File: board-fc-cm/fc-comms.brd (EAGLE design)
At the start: 100 x 100 mm, 231 parts, among them IC1 TXB0108PW, IC10 LNA_COMMON, IC2 LHA1+, IC3 MMZ09332BT1, IC4 PCT2075TP, IC5 PCT2075TP, IC6 MSP430FR2311PW, IC7 CC1125RHBT, IC8 CC1125RHBT, IC9 TXB0108PW, J1 SWD_SHROUD, Q1 8MHz, Q2 BSS84, Q3 32.768kHz, Q4 BSS123, Q5 BSS84, U1 TM4C123[7,G]XXPM, U2 TMP100-EP_DBV_6, U3 TPS3813K33-EP_DBV_6, U4 MPU-9250, U6 TPS79930QDDCRQ1, U7 TPS79930QDDCRQ1, U8 74LVC1G08, X1 BU-SMA-V, X10 BU-SMA-V, X11 BU-SMA-V, X12 BU-SMA-V, X14 BU-SMA-V, X15 BU-SMA-V, X16 BU-SMA-V, X17 BU-SMA-V, X18 SHIELD-26X26, X19 SHIELD-26X26, X2 BU-SMA-V, X20 LFTCXO070, X21 LFTCXO070, X3 BU-SMA-V, X4 BU-SMA-V, X5 BU-SMA-V, X6 BU-SMA-V, X7 BU-SMA-V, X8 BU-SMA-V, X9 BU-SMA-V

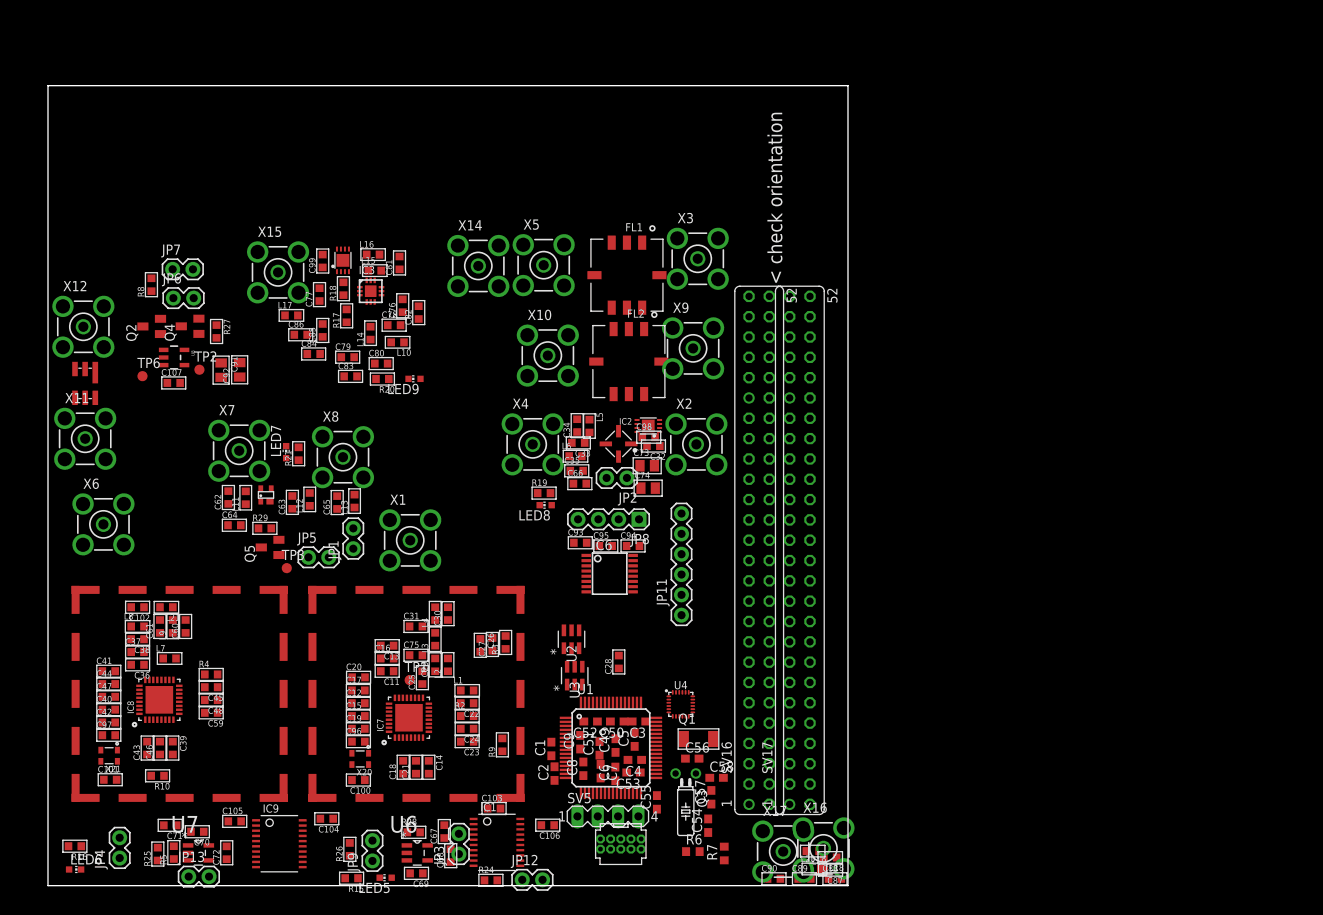
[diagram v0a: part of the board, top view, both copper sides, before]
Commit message: added outline and corrected header locations
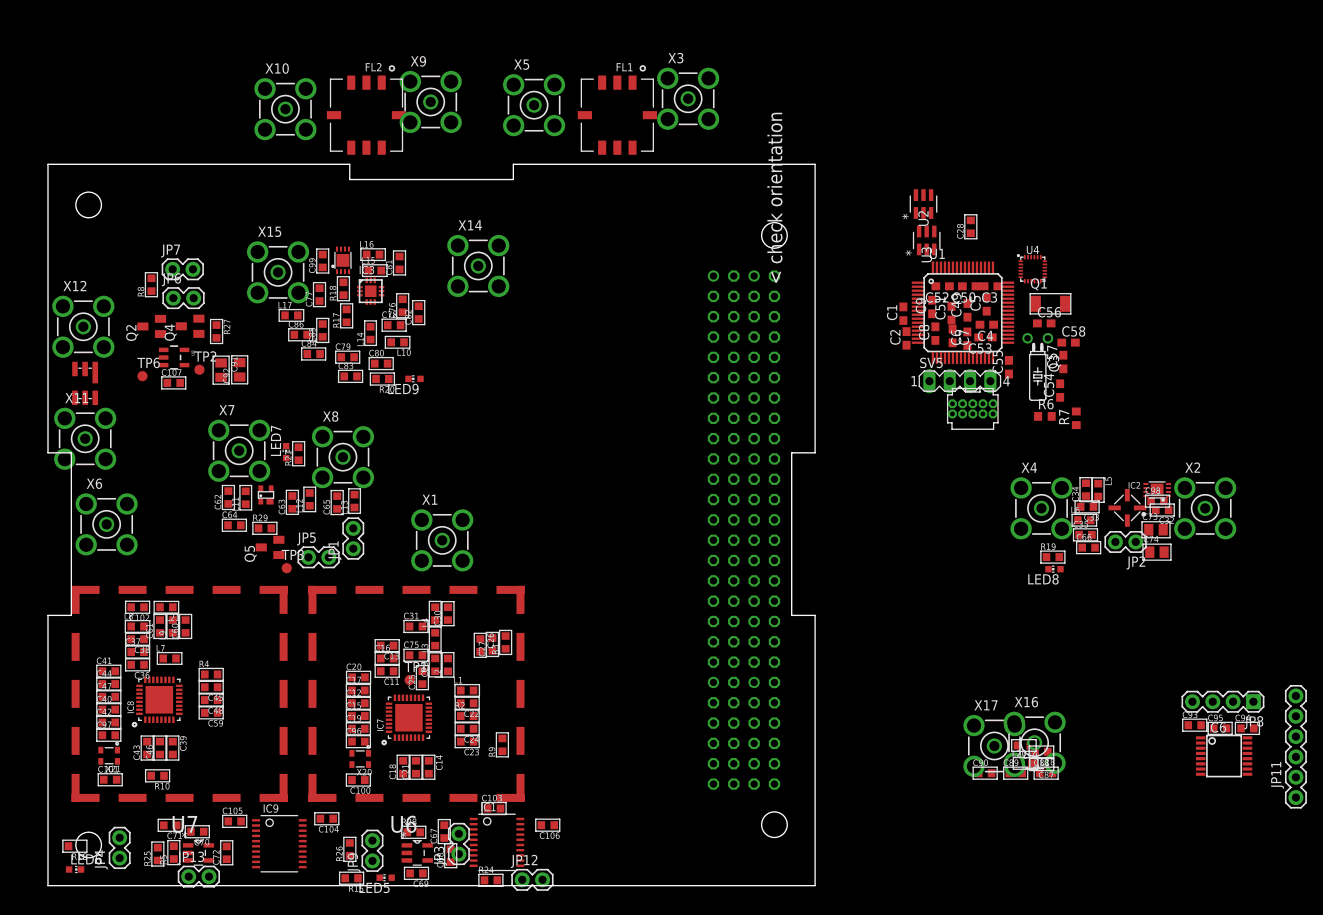
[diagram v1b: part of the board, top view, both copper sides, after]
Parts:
- added U$1: (no value), CubeSat3:OUTLINE
- moved C94 80.1 mm to (149.9, 19.7)
- moved C95 80.1 mm to (146.5, 19.7)
- moved JP11 80.1 mm to (156.0, 11.0)
- moved JP8 80.1 mm to (150.7, 23.0)
- moved C93 80.1 mm to (143.3, 20.1)
- moved IC6 80.1 mm to (147.0, 16.2)
- moved C3 70.0 mm to (117.9, 74.9)
- moved C4 70.0 mm to (117.3, 70.1)
- moved C50 70.0 mm to (115.2, 74.9)
- moved C51 70.0 mm to (112.9, 71.6)
- moved C52 70.0 mm to (111.8, 74.9)
- moved C53 70.0 mm to (117.2, 68.5)
- moved C55 70.0 mm to (120.1, 64.8)
- moved C57 70.0 mm to (126.9, 65.5)
- moved C6 70.0 mm to (114.9, 68.4)
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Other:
- board size 100 x 100 mm -> 95.9 x 90.2 mm

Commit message: more placement
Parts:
- added IC12: TXB0108PW, cube-parts:TSSOP20
- C1, C2, C3, C4, C49, C5, C50, C51, C52, C53, C54, C55, C56, C57, C58, C6, C7, C8, C9: device resistor:C0603 -> passives-7351:C0603-N
- R6, R7: device resistor:R0603 -> passives-7351:R0603-N
- moved C28 81.4 mm to (54.4, 28.4)
- moved C93 77.1 mm to (67.9, 3.74), turned to 90 degrees
- moved IC6 74.9 mm to (73.0, 4.60)
- moved C94 72.4 mm to (78.7, 6.73), turned to 90 degrees
- moved C54 69.7 mm to (63.7, 31.7), turned to 180 degrees
- moved C95 69.5 mm to (78.7, 4.12), turned to 90 degrees
- moved U4 67.7 mm to (60.0, 52.4), turned to 270 degrees
- moved C58 65.3 mm to (64.8, 50.0)
- moved C3 65.2 mm to (56.8, 52.0), turned to 270 degrees
- moved Q1 63.4 mm to (67.1, 47.7), turned to 180 degrees
- moved C6 61.7 mm to (60.8, 38.8), turned to 180 degrees
- moved C4 61.6 mm to (59.6, 48.8), turned to 0 degrees
- moved JP8 61.5 mm to (92.7, 2.59)
- moved C7 61.0 mm to (60.8, 37.2), turned to 180 degrees
- moved C57 60.9 mm to (68.0, 50.0), turned to 180 degrees
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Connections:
- removed net GND1: J1.3
- removed net GND2: J1.5
- removed net GNDD: J1.9
- removed net VCC: J1.1
- net !RST: now also J1.10
- net 3V3/FMCU: now also J1.1
- net GND: now also IC12.11, J1.3, J1.5, J1.9
- net SWCLK: now also J1.4
- net SWDIO: now also J1.2
- net SWO: now also J1.6
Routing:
- net SWO: track 0.00 -> 75.3 mm
- net SWCLK: track 0.00 -> 69.9 mm, vias 0 -> 1
- net !RST: track 0.00 -> 64.7 mm, vias 0 -> 1
- net GPIO4: track 0.00 -> 63.9 mm
- net GPIO3: track 0.00 -> 59.9 mm, vias 0 -> 1
- net GPIO1: track 0.00 -> 59.3 mm, vias 0 -> 1
- net GPIO5: track 0.00 -> 57.5 mm, vias 0 -> 1
- net GPIO2: track 0.00 -> 50.8 mm
- net N$63: track 0.00 -> 36.3 mm, vias 0 -> 1
- net PWR/INT: track 0.00 -> 30.0 mm, vias 0 -> 1
- net SWDIO: track 0.00 -> 30.0 mm
- net PWR/TXD: track 0.00 -> 26.8 mm, vias 0 -> 1
- net PWR/RXD: track 0.00 -> 25.9 mm, vias 0 -> 1
- net GND: track 0.00 -> 16.6 mm, vias 0 -> 4
- net N$101: track 0.00 -> 15.0 mm
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
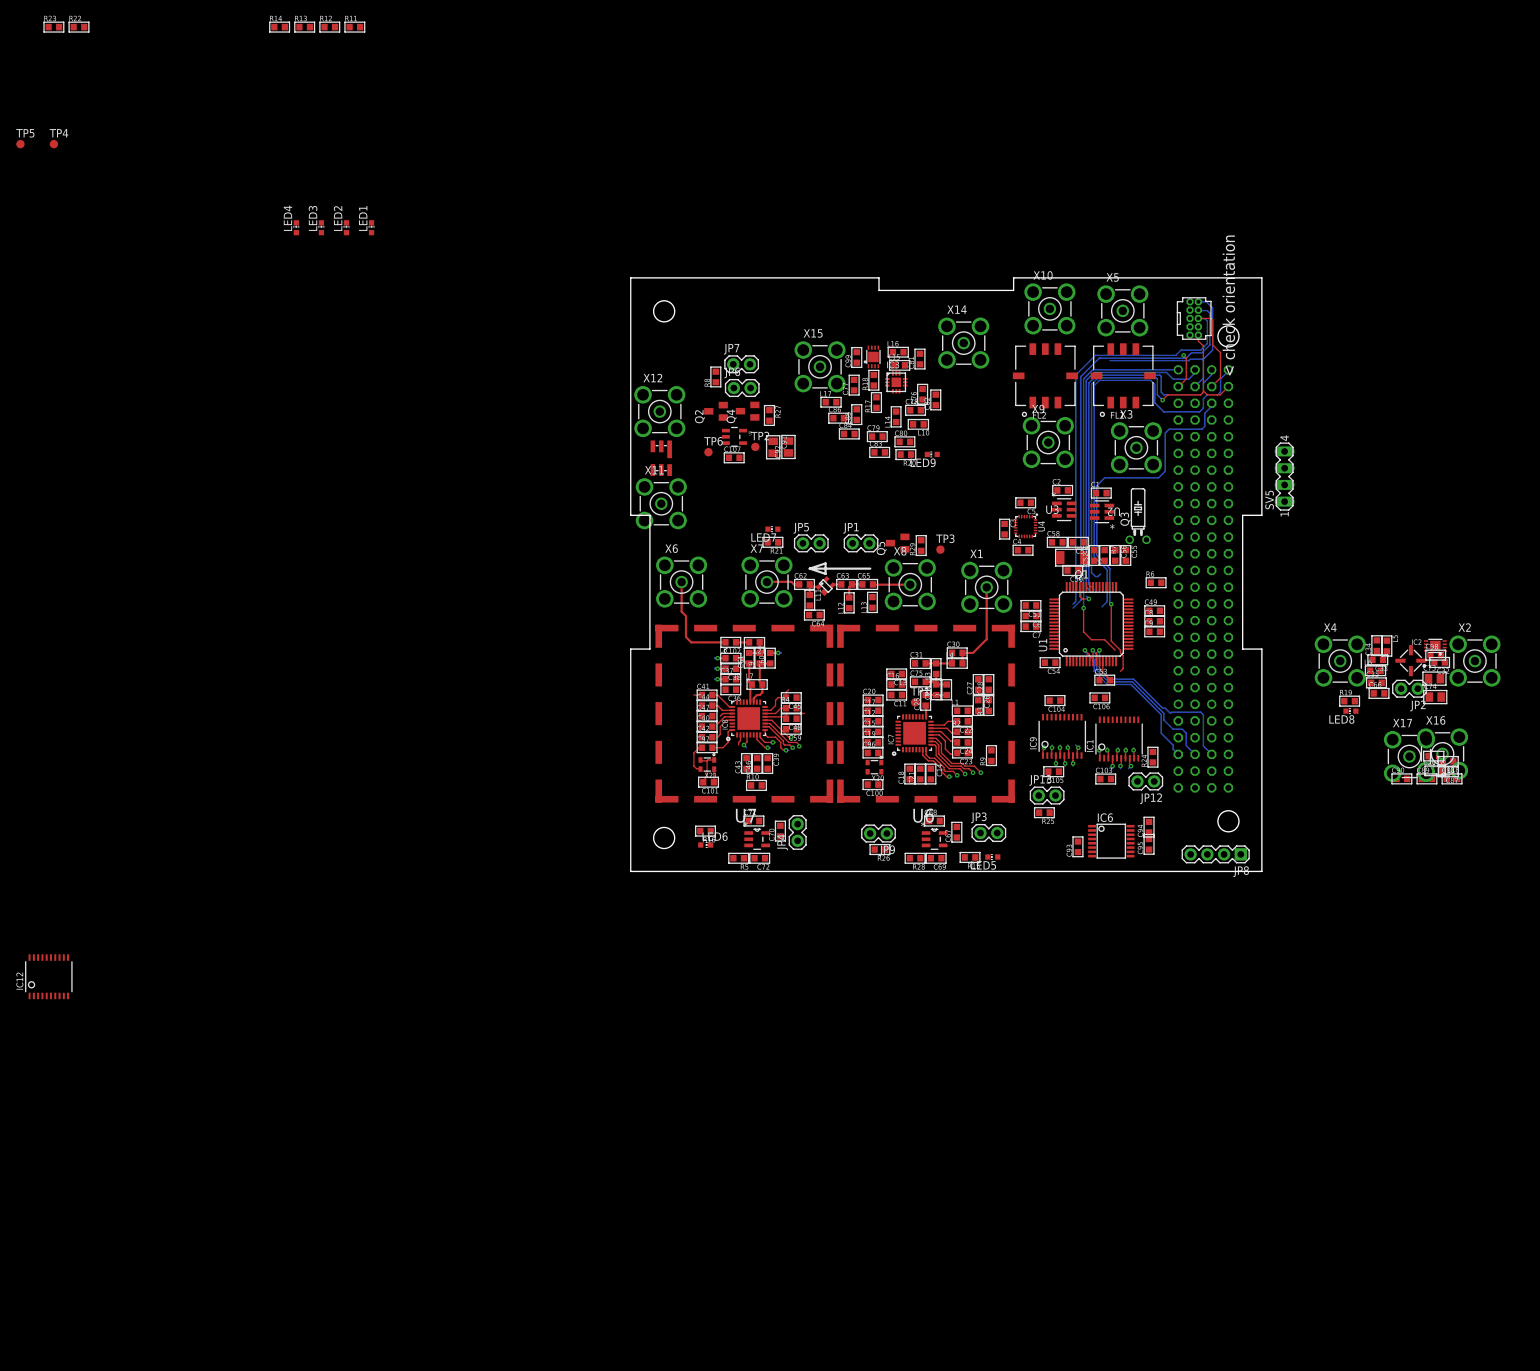
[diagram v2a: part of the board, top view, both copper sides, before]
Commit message: add digital wired up
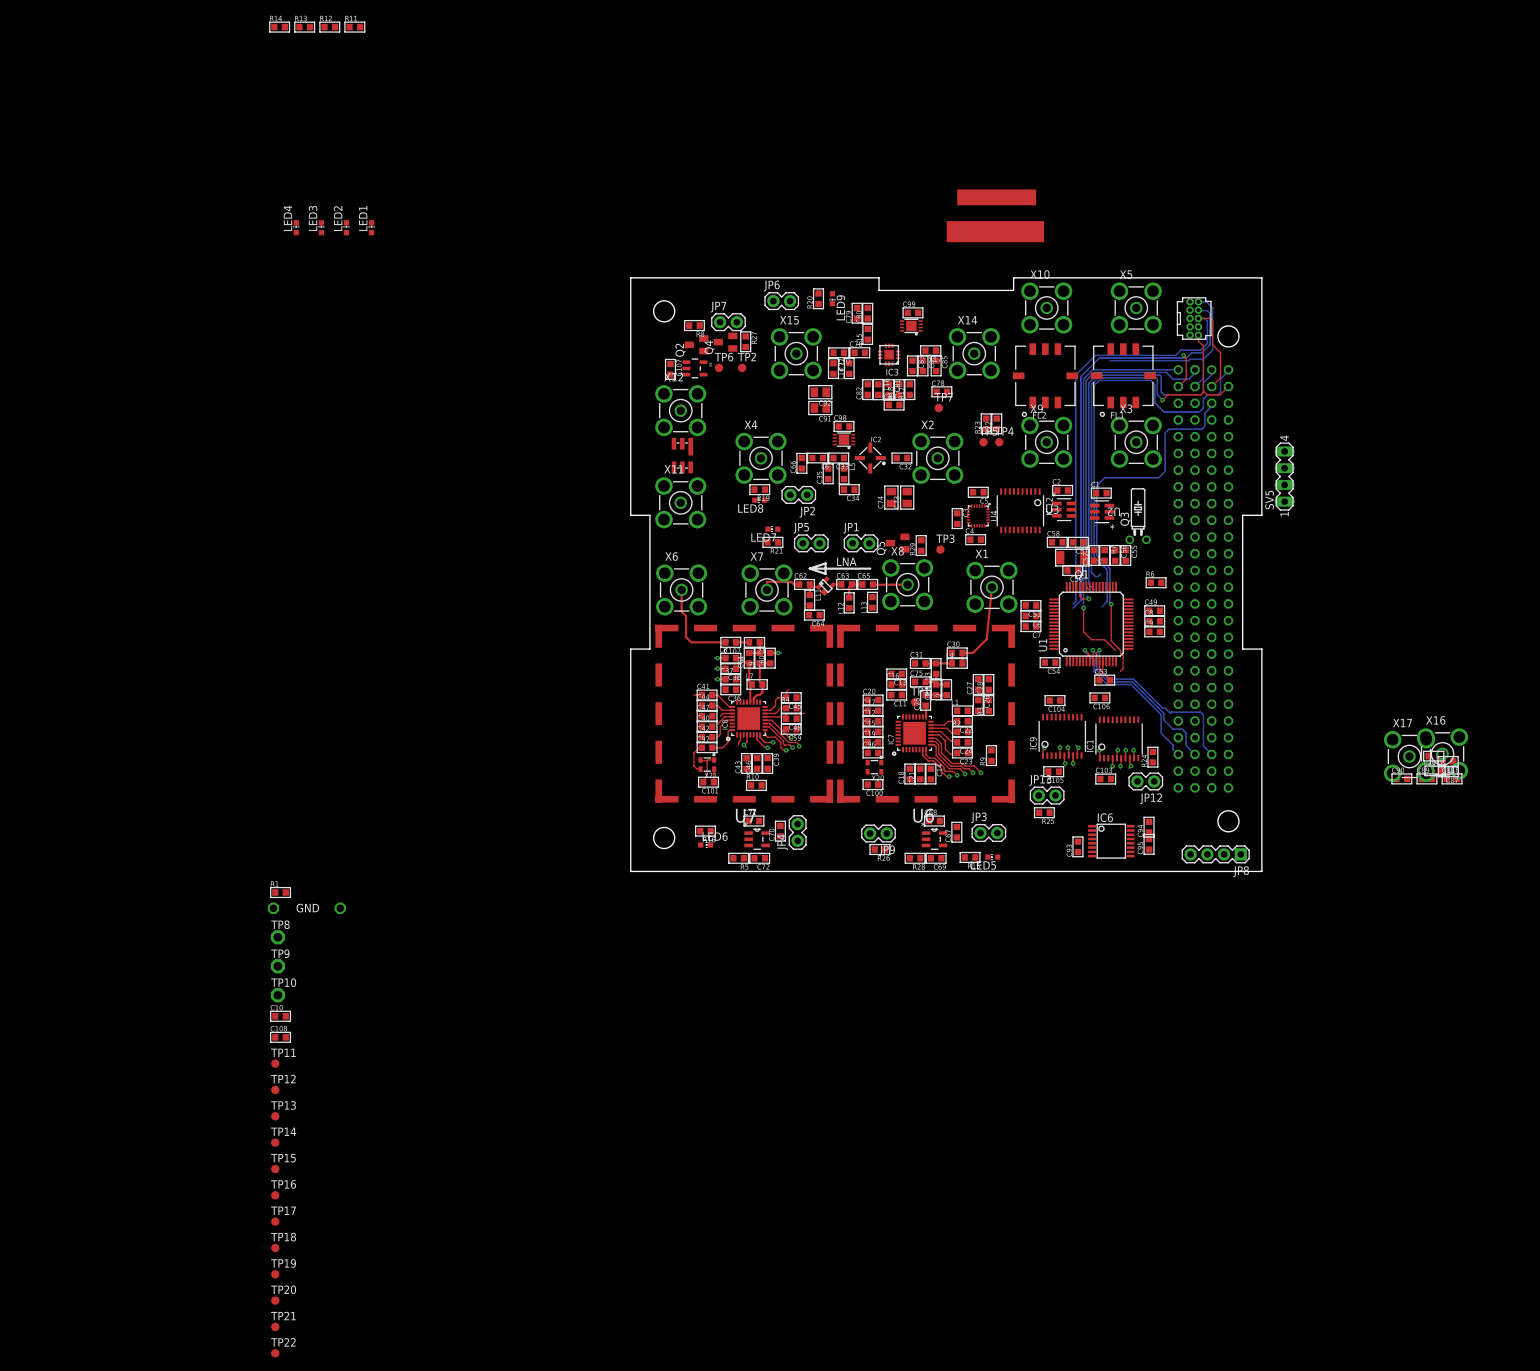
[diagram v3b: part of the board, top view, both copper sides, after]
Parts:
- added C10, C108: 0.1u, passives-7351:C0603-N
- added G1: GND-LOOPL, dtb:GND-LOOP-0.4
- added R1: 10k, passives-7351:R0603-N
- added TP10, TP8, TP9: PTR1PAD1-13, testpad:P1-13
- added TP11, TP12, TP13, TP14, TP15, TP16, TP17, TP18, TP19, TP20, TP21, TP22, TP7: PTR1B1,27, testpad:B1,27
- moved IC12 163.7 mm to (59.2, 54.8), turned to 180 degrees
- moved R23 153.9 mm to (54.0, 68.0), turned to 90 degrees
- moved TP5 153.2 mm to (53.6, 65.2)
- moved R22 151.9 mm to (55.6, 68.0), turned to 90 degrees
- moved TP4 150.6 mm to (56.0, 65.2)
- moved JP2 97.3 mm to (26.8, 57.2)
- moved C98 96.4 mm to (32.4, 67.6)
- moved LED8 95.4 mm to (19.6, 56.4)
- moved R19 95.2 mm to (19.6, 58.0), turned to 180 degrees
- moved IC5 95.1 mm to (32.4, 65.6)
- moved C66 94.4 mm to (26.0, 62.0), turned to 90 degrees
- moved X4 93.2 mm to (19.8, 62.8)
- moved L6 90.7 mm to (28.4, 62.8), turned to 180 degrees
- moved C35 89.1 mm to (30.0, 60.4), turned to 90 degrees
- moved C74 88.0 mm to (39.6, 56.8), turned to 90 degrees
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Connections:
- removed net ?????: R5.1, U7.3
- removed net ??????: R28.1, U6.3
- removed net N$38: JP2.2, JP6.2, JP7.2, Q2.3
- removed net TC/RX/CLK: IC9.14, U1.19
- removed net TC/RX/MISO: IC9.15, U1.21
- removed net TC/RX/MOSI: IC9.16, U1.22
- removed net TC/RX/RST: IC9.12, U1.4
- removed net TC/TX/CLK: IC1.14, U1.30
- removed net TC/TX/MISO: IC1.15, U1.28
- removed net TC/TX/MOSI: IC1.16, U1.29
- removed net TC/TX/RST: IC1.17, U1.1
- new net N$1: IC6.9, R1.2
- new net N$61: IC12.17, SV5.3
- new net PA_POWER: C78.1, IC3.6, TP7.TP, U1.61
- new net PA_PWR: JP2.2, JP6.2, JP7.2, Q2.3, R1.1
- new net RX/GPIO0: IC9.20, U1.4
- new net RX_REG_EN: R5.1, U1.23, U7.3
- new net TC/TXRX/CLK: IC1.14, IC9.14, U1.30
- new net TC/TXRX/MISO: IC1.15, IC9.15, U1.28
- new net TC/TXRX/MOSI: IC1.16, IC9.16, U1.29
- new net TC/TXRX/RST: IC1.17, IC9.12, U1.1
- new net TX/GPIO0: IC1.20, U1.19
- new net TX/WDT/ACK: IC1.18, U1.21
- new net TX/WDT/ERR: IC1.12, U1.22
- new net TX_REG_EN: R28.1, U1.24, U6.3
- net 3V3/FMCU: now also C10.1, IC12.10, IC12.2, TP9.TP
- net 5V/CAM: now also C108.1, IC12.19, TP8.TP
- net CAM/RXD: now also IC12.4
- net CAM/TXD: now also IC12.5
- net GND: now also C10.2, C108.2, G1.P$3, G1.P$4
- net N$73: now also IC12.16, SV5.2; no longer C78.1, IC3.6
- net RX_CLK: now also TP13.TP
- net RX_CS: now also TP12.TP
- net RX_GPIO0: now also TP16.TP
- net RX_GPIO2: no longer IC9.3
- net RX_GPIO3: no longer IC9.4
- net RX_MISO: now also TP14.TP
- net RX_MOSI: now also TP15.TP
- net RX_RST: now also TP11.TP
- net TX_CLK: now also TP19.TP
- net TX_CS: now also TP18.TP
- net TX_GPIO0: now also TP22.TP
- net TX_GPIO2: no longer IC1.3
- net TX_MISO: now also TP21.TP
- net TX_MOSI: now also TP20.TP
- net TX_RST: now also TP17.TP
- net WDT_ACK: now also IC1.3
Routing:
- net TX_GPIO2: track 1.67 -> 0.00 mm, vias 1 -> 0
- net RX_GPIO2: track 3.92 -> 2.30 mm, vias 2 -> 1
- net RX_GPIO3: track 1.41 -> 0.00 mm, vias 1 -> 0
- net N$101: track 15.0 -> 13.8 mm
- net N$17: track 5.08 -> 6.27 mm
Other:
- board text added: "LNA"
- board text removed: "< check orientation"

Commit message: started routing
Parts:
- removed JP4: M02PTH, SparkFun-Connectors:1X02
- added C109, C110: 4.7u, passives-7351:C0603-N
- added J2, J3: (no value), dtb:JST-2-TH
- added R30: 0.2, passives-7351:R0603-N
- added U$2: MCP1700TT, dtb:SOT23
- moved TP8 152.7 mm to (94.0, 29.2)
- moved TP9 152.4 mm to (94.0, 23.6)
- moved TP10 152.1 mm to (94.0, 18.0)
- moved G1 81.3 mm to (31.6, 3.60)
- moved JP3 41.5 mm to (11.6, 6.40), turned to 270 degrees
- moved JP8 22.4 mm to (70.3, 2.19)
- moved R9 13.1 mm to (42.0, 14.8), turned to 270 degrees
- moved C94 8.99 mm to (70.3, 9.93)
- moved C95 8.74 mm to (70.3, 6.52)
- moved IC6 8.59 mm to (65.4, 8.60)
- moved JP13 7.90 mm to (60.1, 19.2), turned to 90 degrees
- moved C93 7.69 mm to (61.1, 7.34)
- moved LED6 7.38 mm to (5.79, 8.82)
- moved R15 7.21 mm to (58.4, 4.53)
- moved R25 6.26 mm to (60.4, 14.7), turned to 0 degrees
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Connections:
- removed net N$51: C100.1, C103.1, C107.1, C12.2, C15.2, C16.2, C17.2, C18.2, C19.2, C20.2, C21.2, C22.2, C23.2, C24.2, C26.1, C27.1, C28.1, C93.1, C94.1, C95.1, IC1.2, IC6.5, IC7.1, IC7.12, IC7.13, IC7.15, IC7.22, IC7.25, IC7.26, IC7.27, IC7.28, IC7.29, IC7.5, JP3.2, JP8.1, R24.2, R3.2, R9.2, U8.5, X20.6
- removed net N$59: C70.1, U7.5
- removed net N$63: C101.1, C105.1, C37.2, C40.2, C41.2, C42.2, C43.2, C44.2, C45.2, C46.2, C47.2, C48.2, C59.2, IC8.1, IC8.12, IC8.13, IC8.15, IC8.22, IC8.25, IC8.26, IC8.27, IC8.28, IC8.29, IC8.5, IC9.2, JP4.1, R10.2, R25.2, X21.6
- new net EWFEWF: C71.1, JP3.1, R30.2, R5.2, U7.1
- net 3V3/FMCU: now also C110.1, U$2.2
- net 5V/CAM: now also J3.1
- net 5V/SYS: now also C109.1, J2.1, JP3.2, R30.1, TP10.TP, U$2.3; no longer C71.1, R5.2, U7.1
- net GND: now also C109.2, C110.2, J2.2, J3.2, U$2.1, X11.2, X11.3, X11.4, X11.5, X12.2, X12.3, X12.4, X12.5
- net N$40: now also C100.1, C103.1, C107.1, C12.2, C15.2, C16.2, C17.2, C18.2, C19.2, C20.2, C21.2, C22.2, C23.2, C24.2, C26.1, C27.1, C28.1, C93.1, C94.1, C95.1, IC1.2, IC6.5, IC7.1, IC7.12, IC7.13, IC7.15, IC7.22, IC7.25, IC7.26, IC7.27, IC7.28, IC7.29, IC7.5, JP8.1, R24.2, R3.2, R9.2, U8.5, X20.6; no longer JP3.1
- net N$53: now also C101.1, C105.1, C37.2, C40.2, C41.2, C42.2, C43.2, C44.2, C45.2, C46.2, C47.2, C48.2, C59.2, C70.1, IC8.1, IC8.12, IC8.13, IC8.15, IC8.22, IC8.25, IC8.26, IC8.27, IC8.28, IC8.29, IC8.5, IC9.2, R10.2, R25.2, U7.5, X21.6; no longer JP4.2
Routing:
- net GND: track 16.6 -> 139.8 mm, vias 4 -> 114
- net RX_REG_EN: track 0.00 -> 116.1 mm, vias 0 -> 1
- net N$40: track 0.00 -> 103.5 mm, vias 0 -> 15
- net N$53: track 0.00 -> 102.7 mm, vias 0 -> 13
- net N$63: track 36.3 -> 0.00 mm, vias 1 -> 0
- net N$52: track 0.00 -> 15.2 mm, vias 0 -> 1
- net N$51: track 12.5 -> 0.00 mm
- net 5V/SYS: track 0.00 -> 9.59 mm
- net EWFEWF: track 0.00 -> 9.35 mm
- net N$102: track 0.00 -> 8.90 mm
- net RX_RST: track 3.49 -> 11.5 mm, vias 1 -> 2
- net N$14: track 0.00 -> 7.87 mm, vias 0 -> 1
- net N$11: track 0.00 -> 7.21 mm
- net TX_RST: track 1.61 -> 8.49 mm, vias 1 -> 2
- net N$15: track 0.00 -> 6.73 mm
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- added copper zone on layer 1, net GND
- added copper zone on layer 15, net N$2
- added copper zone on layer 15, net N$53
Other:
- board text added: "MHz"
- board text added: "RX"
- board text added: "TX"
